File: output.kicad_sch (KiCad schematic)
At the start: 32 parts, among them J1 SMA, J2 SMA, J3 SMA, J4 SMA, J5 U.Fl, T1 MABA-007159-000000, T2 MABA-007159-000000, U12 74LVC1G125, U13 74CB3Q3306

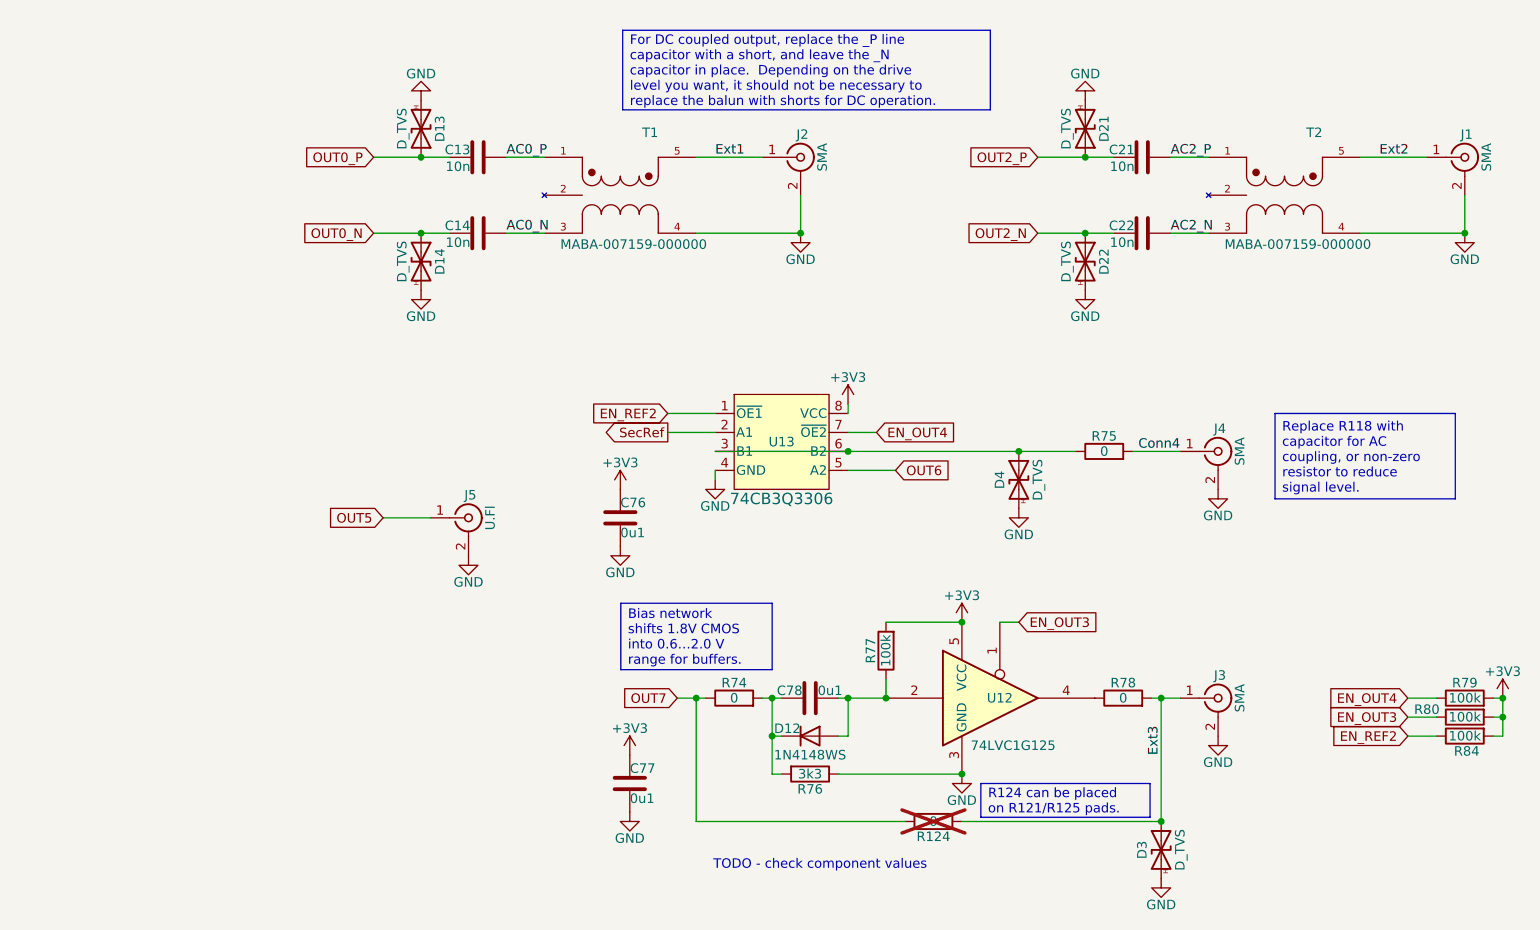
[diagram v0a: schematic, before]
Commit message: DRC clean-up.  Only silk-screen noise left.
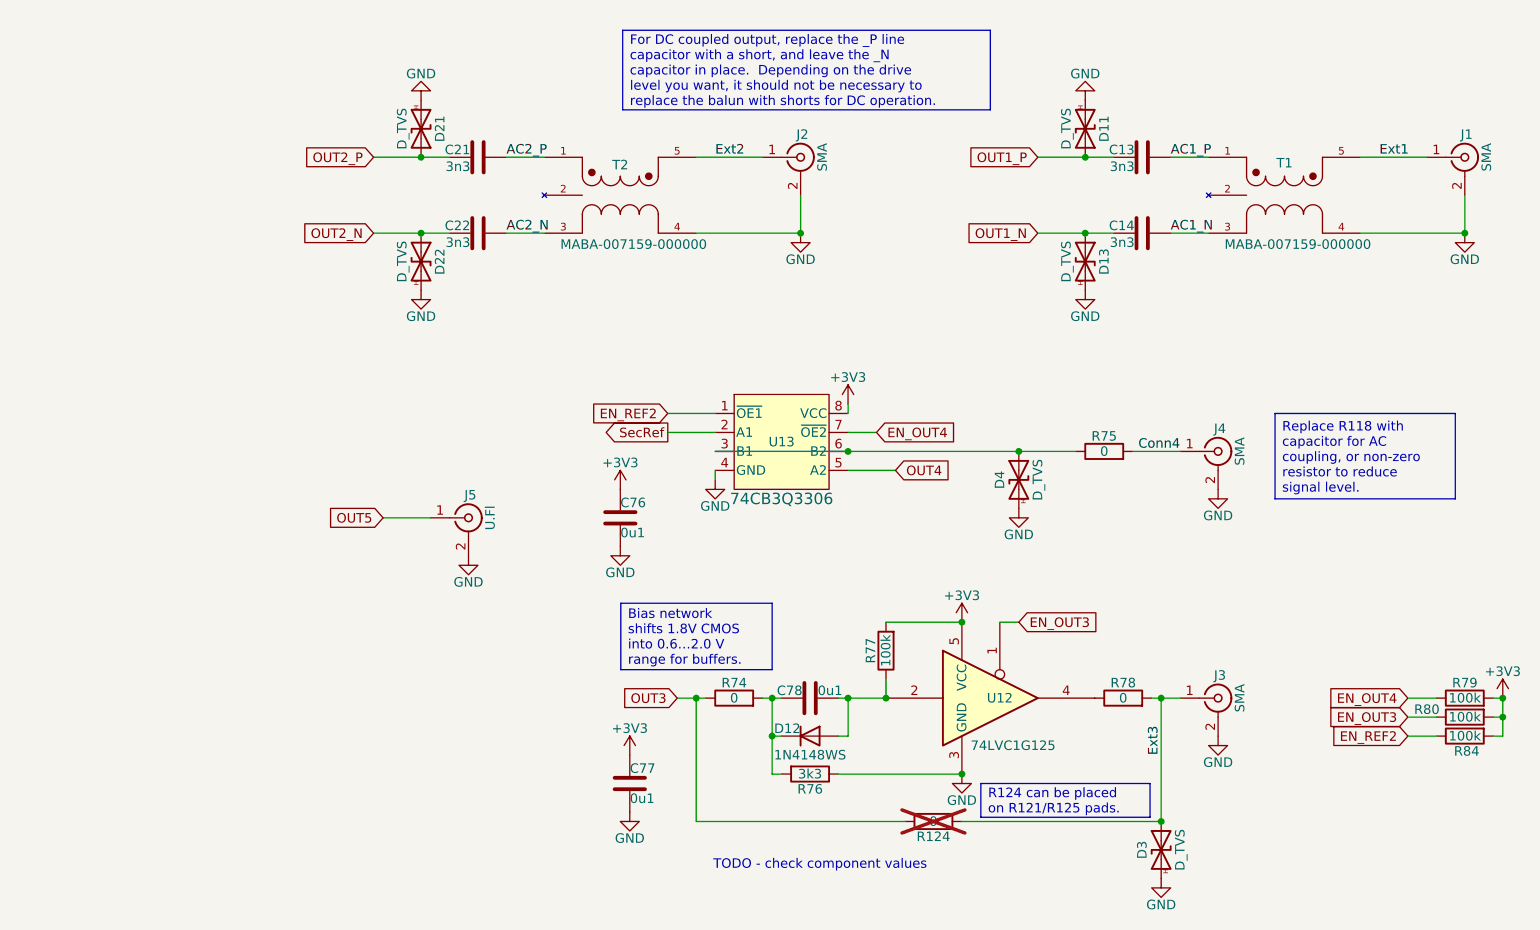
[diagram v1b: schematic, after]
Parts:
- C13: renamed from C21; value 10n -> 3n3; JLCPCB C15195 -> C26404
- C14: renamed from C22; value 10n -> 3n3; JLCPCB C15195 -> C26404
- C21: renamed from C13; value 10n -> 3n3; JLCPCB C15195 -> C26404
- C22: renamed from C14; value 10n -> 3n3; JLCPCB C15195 -> C26404
- J1, J2, J3, J4: footprint Connector_Coaxial:SMA_Amphenol_132289_EdgeMount -> Parts:SMA_Amphenol_132289_EdgeMount
- J5: footprint Connector_Coaxial:U.FL_Hirose_U.FL-R-SMT-1_Vertical -> Parts:U.FL_Hirose_U.FL-R-SMT-1_Vertical
- renumbered D21 to D11, D22 to D13, D13 to D21, D14 to D22, T2 to T1, T1 to T2
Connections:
- net AC0_N is gone; now on net AC2_N: C22.2, T2.3
- net AC0_P is gone; now on net AC2_P: C21.2, T2.1
- net OUT0_N is gone; now on net OUT2_N: C22.1, D22.1 (A1)
- net OUT0_P is gone; now on net OUT2_P: C21.1, D21.1 (A1)
- net AC2_N: no longer C14.2, T1.3
- net AC2_P: no longer C13.2, T1.1
- net Ext1: now also J1.1 (In), T1.5; no longer J2.1 (In), T2.5
- net Ext2: now also J2.1 (In), T2.5; no longer J1.1 (In), T1.5
- net OUT2_N: no longer C14.1, D13.1 (A1)
- net OUT2_P: no longer C13.1, D11.1 (A1)
- net OUT6 renamed OUT4
- net OUT7 renamed OUT3
- new net AC1_N: C14.2, T1.3
- new net AC1_P: C13.2, T1.1
- new net OUT1_N: C14.1, D13.1 (A1)
- new net OUT1_P: C13.1, D11.1 (A1)
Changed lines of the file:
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@@
 		)
 	)
-	(label "AC2_P"
+	(label "AC1_P"
 		(at 194.31 53.34 0)
 		(effects
@@
 		)
 	)
-	(label "AC0_N"
+	(label "AC2_N"
 		(at 105.41 63.5 0)
 		(effects
@@
 		)
 	)
-	(label "Ext1"
+	(label "Ext2"
 		(at 133.35 53.34 0)
 		(effects
@@
 		)
 	)
-	(label "AC0_P"
+	(label "AC2_P"
 		(at 105.41 53.34 0)
 		(effects
@@
 		)
 	)
-	(label "Ext2"
+	(label "Ext1"
 		(at 222.25 53.34 0)
 		(effects
@@
 		)
 	)
-	(label "AC2_N"
+	(label "AC1_N"
 		(at 194.31 63.5 0)
 		(effects
@@
 		)
 	)
-	(global_label "OUT0_P"
+	(global_label "OUT2_P"
 		(shape input)
 		(at 87.63 53.34 180)
@@
 		)
 	)
-	(global_label "OUT2_N"
+	(global_label "OUT1_N"
 		(shape input)
 		(at 176.53 63.5 180)
@@
 		)
 	)
-	(global_label "OUT6"
+	(global_label "OUT4"
 		(shape input)
 		(at 157.48 95.25 0)
@@
 		)
 	)
-	(global_label "OUT7"
+	(global_label "OUT3"
 		(shape input)
 		(at 128.27 125.73 180)
@@
 		)
 	)
-	(global_label "OUT0_N"
+	(global_label "OUT2_N"
 		(shape input)
 		(at 87.63 63.5 180)
@@
 		)
 	)
-	(global_label "OUT2_P"
+	(global_label "OUT1_P"
 		(shape input)
 		(at 176.53 53.34 180)
@@
 		(on_board yes)
 		(dnp no)
-		(property "Reference" "D14"
+		(property "Reference" "D22"
 			(at 96.52 67.31 0)
 			(effects
@@
 			(project "gpsref"
 				(path "/3160ff17-81c2-4674-af97-e8d9acaf6b65/26994282-45a2-461a-b033-dde2ded4d8ff"
-					(reference "D14")
+					(reference "D22")
 					(unit 1)
 				)
@@
 		(on_board yes)
 		(dnp no)
-		(property "Reference" "C13"
+		(property "Reference" "C21"
 			(at 100.584 53.086 90)
 			(effects
@@
 			)
 		)
-		(property "Value" "10n"
+		(property "Value" "3n3"
 			(at 100.584 53.848 90)
 			(effects
@@
 			)
 		)
-		(property "JLCPCB" "C15195"
+		(property "JLCPCB" "C26404"
 			(at 101.6 53.34 0)
 			(effects
@@
 			(project "gpsref"
 				(path "/3160ff17-81c2-4674-af97-e8d9acaf6b65/26994282-45a2-461a-b033-dde2ded4d8ff"
-					(reference "C13")
+					(reference "C21")
 					(unit 1)
 				)
@@
 			)
 		)
-		(property "Footprint" "Connector_Coaxial:SMA_Amphenol_132289_EdgeMount"
+		(property "Footprint" "Parts:SMA_Amphenol_132289_EdgeMount"
 			(at 200.66 125.73 0)
 			(effects
@@
 		(on_board yes)
 		(dnp no)
-		(property "Reference" "C22"
+		(property "Reference" "C14"
 			(at 189.484 63.246 90)
 			(effects
@@
 			)
 		)
-		(property "Value" "10n"
+		(property "Value" "3n3"
 			(at 189.484 64.008 90)
 			(effects
@@
 			)
 		)
-		(property "JLCPCB" "C15195"
+		(property "JLCPCB" "C26404"
 			(at 190.5 63.5 0)
 			(effects
@@
 			(project "gpsref"
 				(path "/3160ff17-81c2-4674-af97-e8d9acaf6b65/26994282-45a2-461a-b033-dde2ded4d8ff"
-					(reference "C22")
+					(reference "C14")
 					(unit 1)
 				)
@@
 		(on_board yes)
 		(dnp no)
-		(property "Reference" "T2"
-			(at 214.6339 50.7921 0)
+		(property "Reference" "T1"
+			(at 209.5539 54.8561 0)
 			(effects
 				(font
 					(size 1.27 1.27)
 				)
-				(justify left bottom)
+				(justify bottom)
 			)
 		)
@@
 			(project "gpsref"
 				(path "/3160ff17-81c2-4674-af97-e8d9acaf6b65/26994282-45a2-461a-b033-dde2ded4d8ff"
-					(reference "T2")
+					(reference "T1")
 					(unit 1)
 				)
@@
 			)
 		)
-		(property "Footprint" "Connector_Coaxial:SMA_Amphenol_132289_EdgeMount"
+		(property "Footprint" "Parts:SMA_Amphenol_132289_EdgeMount"
 			(at 200.66 92.71 0)
 			(effects
@@
 		(on_board yes)
 		(dnp no)
-		(property "Reference" "T1"
-			(at 125.7339 50.7921 0)
+		(property "Reference" "T2"
+			(at 120.6539 55.1101 0)
 			(effects
 				(font
 					(size 1.27 1.27)
 				)
-				(justify left bottom)
+				(justify bottom)
 			)
 		)
@@
 			(project ""
 				(path "/3160ff17-81c2-4674-af97-e8d9acaf6b65/26994282-45a2-461a-b033-dde2ded4d8ff"
-					(reference "T1")
+					(reference "T2")
 					(unit 1)
 				)
@@
 		(on_board yes)
 		(dnp no)
-		(property "Reference" "C14"
+		(property "Reference" "C22"
 			(at 100.584 63.246 90)
 			(effects
@@
 			)
 		)
-		(property "Value" "10n"
+		(property "Value" "3n3"
 			(at 100.584 64.008 90)
 			(effects
@@
 			)
 		)
-		(property "JLCPCB" "C15195"
+		(property "JLCPCB" "C26404"
 			(at 101.6 63.5 0)
 			(effects
@@
 			(project "gpsref"
 				(path "/3160ff17-81c2-4674-af97-e8d9acaf6b65/26994282-45a2-461a-b033-dde2ded4d8ff"
-					(reference "C14")
+					(reference "C22")
 					(unit 1)
 				)
@@
 		(on_board yes)
 		(dnp no)
-		(property "Reference" "D22"
+		(property "Reference" "D13"
 			(at 185.42 67.31 0)
 			(effects
@@
 			(project "gpsref"
 				(path "/3160ff17-81c2-4674-af97-e8d9acaf6b65/26994282-45a2-461a-b033-dde2ded4d8ff"
-					(reference "D22")
+					(reference "D13")
 					(unit 1)
 				)
@@
 		(on_board yes)
 		(dnp no)
-		(property "Reference" "D21"
+		(property "Reference" "D11"
 			(at 185.42 49.53 0)
 			(effects
@@
 			(project "gpsref"
 				(path "/3160ff17-81c2-4674-af97-e8d9acaf6b65/26994282-45a2-461a-b033-dde2ded4d8ff"
-					(reference "D21")
+					(reference "D11")
 					(unit 1)
 				)
@@
 			)
 		)
-		(property "Footprint" "Connector_Coaxial:U.FL_Hirose_U.FL-R-SMT-1_Vertical"
+		(property "Footprint" "Parts:U.FL_Hirose_U.FL-R-SMT-1_Vertical"
 			(at 100.33 101.6 0)
 			(effects
@@
 			)
 		)
-		(property "Footprint" "Connector_Coaxial:SMA_Amphenol_132289_EdgeMount"
+		(property "Footprint" "Parts:SMA_Amphenol_132289_EdgeMount"
 			(at 144.78 53.34 0)
 			(effects
@@
 		(on_board yes)
 		(dnp no)
-		(property "Reference" "D13"
+		(property "Reference" "D21"
 			(at 96.52 49.53 0)
 			(effects
@@
 			(project "gpsref"
 				(path "/3160ff17-81c2-4674-af97-e8d9acaf6b65/26994282-45a2-461a-b033-dde2ded4d8ff"
-					(reference "D13")
+					(reference "D21")
 					(unit 1)
 				)
@@
 		(on_board yes)
 		(dnp no)
-		(property "Reference" "C21"
+		(property "Reference" "C13"
 			(at 189.484 53.086 90)
 			(effects
@@
 			)
 		)
-		(property "Value" "10n"
+		(property "Value" "3n3"
 			(at 189.484 53.848 90)
 			(effects
@@
 			)
 		)
-		(property "JLCPCB" "C15195"
+		(property "JLCPCB" "C26404"
 			(at 190.5 53.34 0)
 			(effects
@@
 			(project "gpsref"
 				(path "/3160ff17-81c2-4674-af97-e8d9acaf6b65/26994282-45a2-461a-b033-dde2ded4d8ff"
-					(reference "C21")
+					(reference "C13")
 					(unit 1)
 				)
@@
 			)
 		)
-		(property "Footprint" "Connector_Coaxial:SMA_Amphenol_132289_EdgeMount"
+		(property "Footprint" "Parts:SMA_Amphenol_132289_EdgeMount"
 			(at 233.68 53.34 0)
 			(effects

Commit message: Squeeze in a connector to break out GPS.
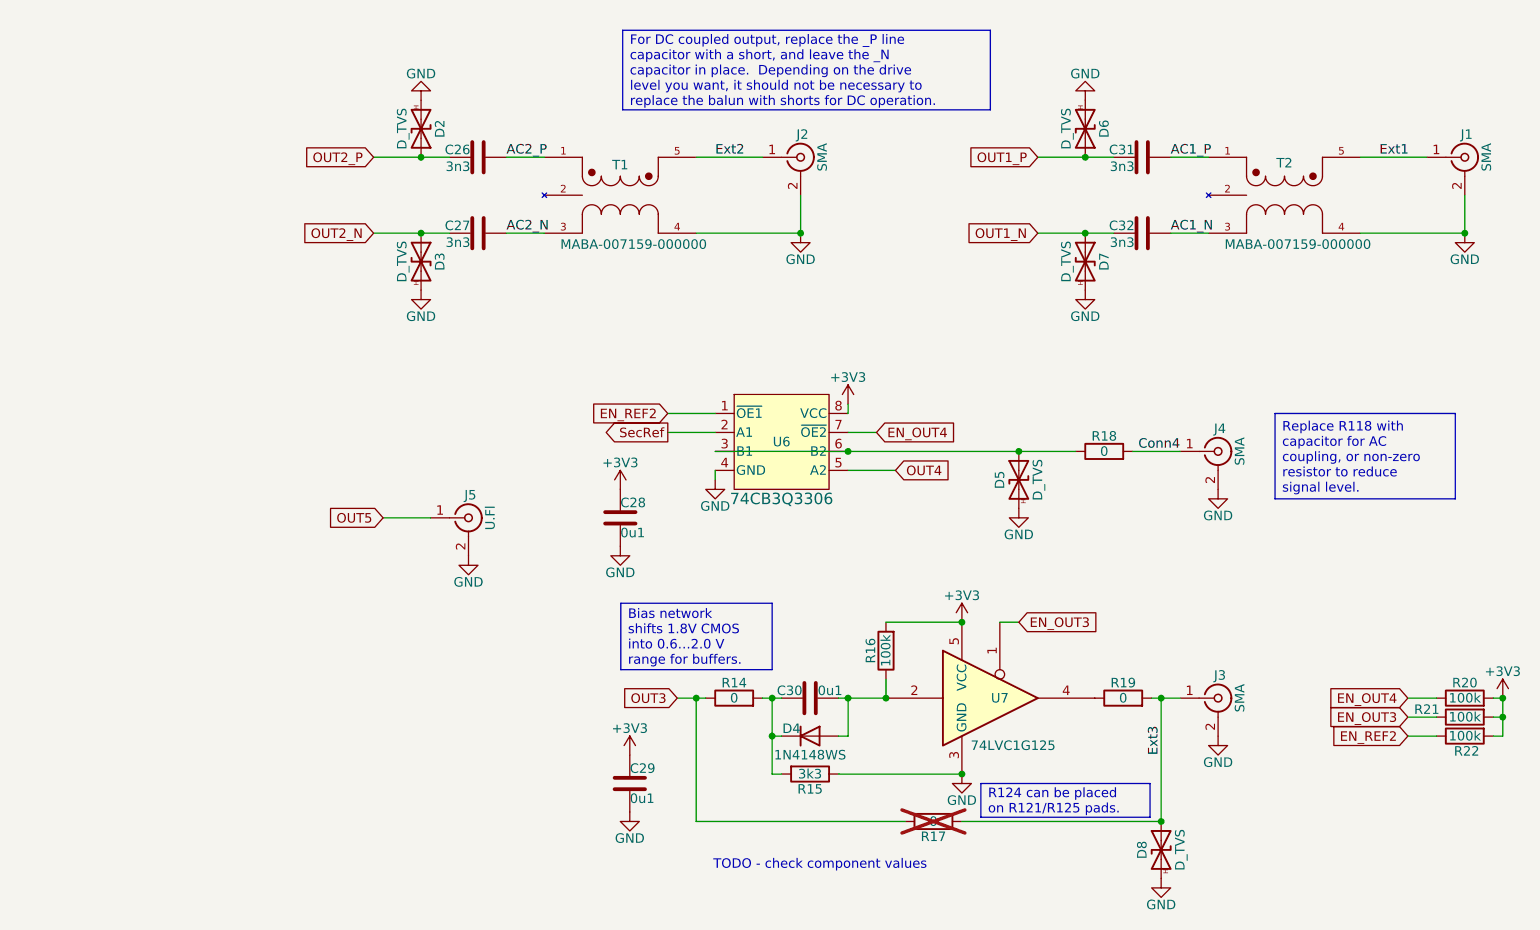
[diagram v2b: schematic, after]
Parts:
- renumbered C21 to C26, C22 to C27, C76 to C28, C77 to C29, C78 to C30, C13 to C31, C14 to C32, D21 to D2, D22 to D3, D12 to D4, D4 to D5, D11 to D6, D13 to D7, D3 to D8, R74 to R14, R76 to R15, R77 to R16, R124 to R17, R75 to R18, R78 to R19, R79 to R20, R80 to R21, R84 to R22, T2 to T1, T1 to T2, U13 to U6, U12 to U7
